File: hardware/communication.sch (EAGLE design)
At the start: 44 parts, among them J1 MICRO_USB_B_HIROSE_ZX62-B-5PA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, SW1 TVAF06-A020B-R, U2 NJM12888F, X1 FA-238

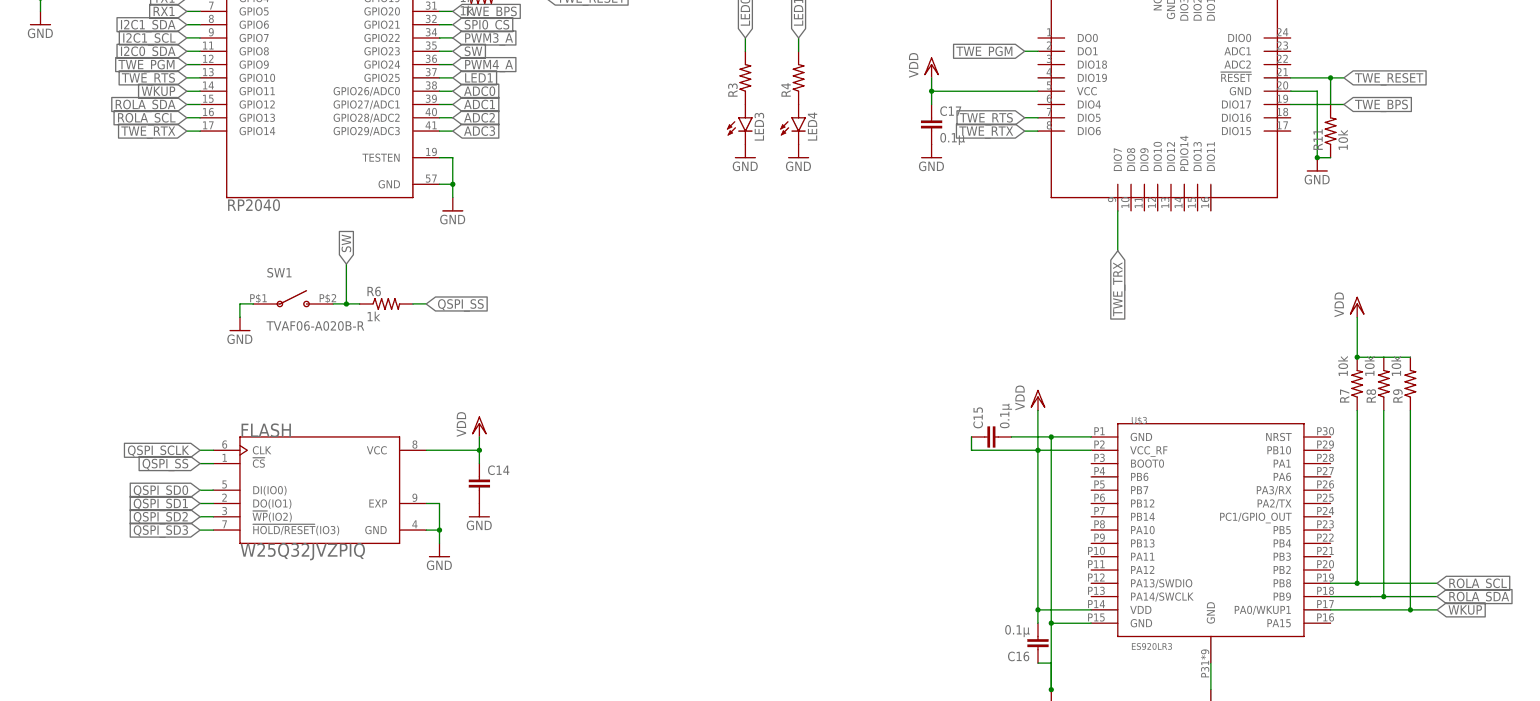
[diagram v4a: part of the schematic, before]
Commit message: 変更点: communication_LoRaをUART接続に変換 gnss_GPSのRTX接続およびRESETの追加
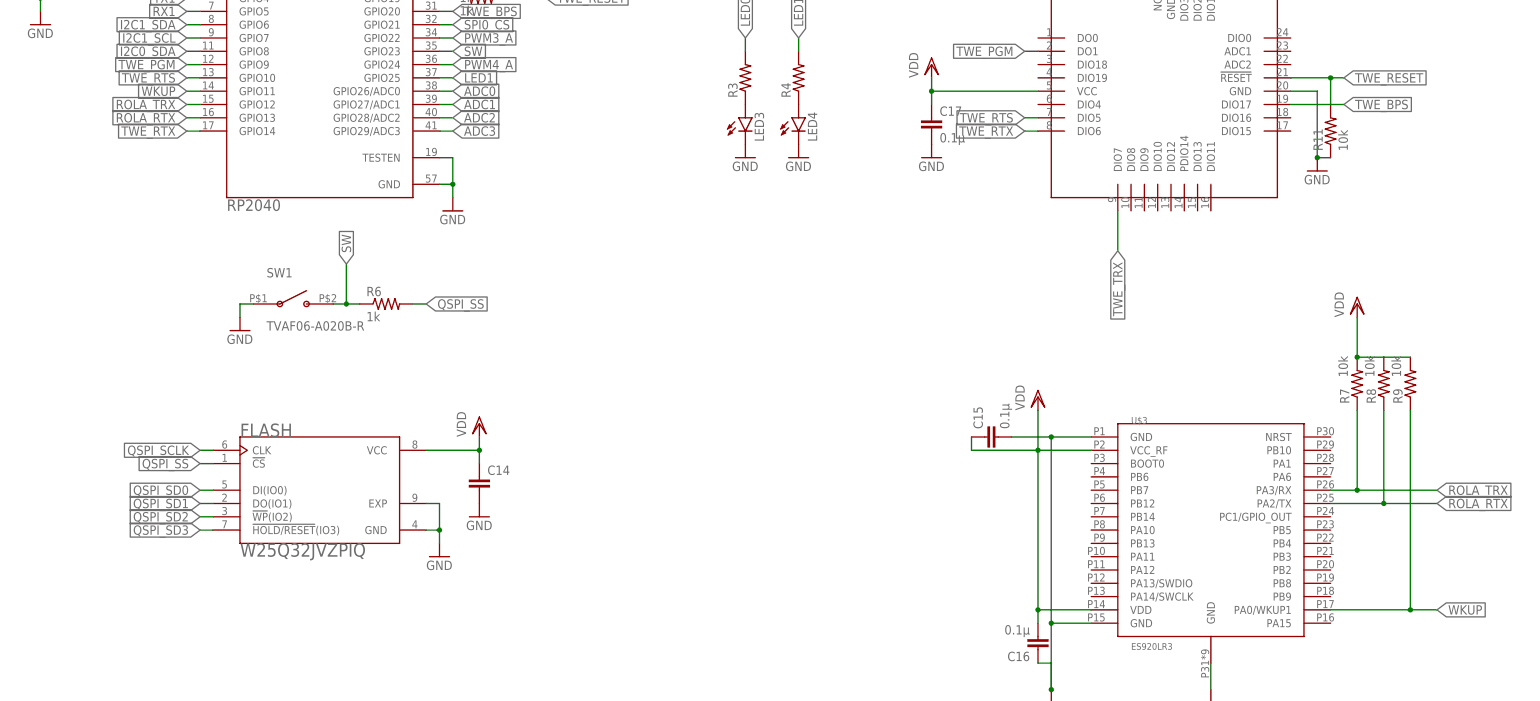
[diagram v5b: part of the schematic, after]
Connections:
- removed net ROLA_SCL: R7.1, RP1.GPIO13, U$3.PB8
- removed net ROLA_SDA: R8.1, RP1.GPIO12, U$3.PB9
- new net ROLA_RTX: R8.1, RP1.GPIO13, U$3.PA2/TX
- new net ROLA_TRX: R7.1, RP1.GPIO12, U$3.PA3/RX
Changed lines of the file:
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@@
-</segment>
-</net>
-<net name="ROLA_SCL" class="0">
-<segment>
-<pinref part="R7" gate="G$1" pin="1"/>
-<pinref part="U$3" gate="G$1" pin="PB8"/>
-<wire x1="248.92" y1="-25.4" x2="254" y2="-25.4" width="0.1524" layer="91"/>
-<label x="269.24" y="-25.4" size="1.778" layer="95" xref="yes"/>
-<wire x1="254" y1="-25.4" x2="269.24" y2="-25.4" width="0.1524" layer="91"/>
-<wire x1="254" y1="7.62" x2="254" y2="-25.4" width="0.1524" layer="91"/>
-<junction x="254" y="-25.4"/>
-</segment>
-<segment>
-<pinref part="RP1" gate="G$1" pin="GPIO13"/>
-<wire x1="33.02" y1="63.5" x2="30.48" y2="63.5" width="0.1524" layer="91"/>
-<label x="30.48" y="63.5" size="1.778" layer="95" rot="R180" xref="yes"/>
-</segment>
-</net>
-<net name="ROLA_SDA" class="0">
-<segment>
-<pinref part="R8" gate="G$1" pin="1"/>
-<pinref part="U$3" gate="G$1" pin="PB9"/>
-<wire x1="248.92" y1="-27.94" x2="256.54" y2="-27.94" width="0.1524" layer="91"/>
-<label x="269.24" y="-27.94" size="1.778" layer="95" xref="yes"/>
-<wire x1="259.08" y1="-27.94" x2="269.24" y2="-27.94" width="0.1524" layer="91"/>
-<wire x1="259.08" y1="7.62" x2="259.08" y2="-27.94" width="0.1524" layer="91"/>
-<wire x1="259.08" y1="-27.94" x2="256.54" y2="-27.94" width="0.1524" layer="91"/>
-<junction x="259.08" y="-27.94"/>
-</segment>
-<segment>
-<pinref part="RP1" gate="G$1" pin="GPIO12"/>
-<wire x1="33.02" y1="66.04" x2="30.48" y2="66.04" width="0.1524" layer="91"/>
-<label x="30.48" y="66.04" size="1.778" layer="95" rot="R180" xref="yes"/>
 </segment>
 </net>
@@
 </segment>
 </net>
+<net name="ROLA_TRX" class="0">
+<segment>
+<pinref part="U$3" gate="G$1" pin="PA3/RX"/>
+<wire x1="248.92" y1="-7.62" x2="254" y2="-7.62" width="0.1524" layer="91"/>
+<pinref part="R7" gate="G$1" pin="1"/>
+<wire x1="254" y1="-7.62" x2="269.24" y2="-7.62" width="0.1524" layer="91"/>
+<wire x1="254" y1="7.62" x2="254" y2="-7.62" width="0.1524" layer="91"/>
+<junction x="254" y="-7.62"/>
+<label x="269.24" y="-7.62" size="1.778" layer="95" xref="yes"/>
+</segment>
+<segment>
+<pinref part="RP1" gate="G$1" pin="GPIO12"/>
+<wire x1="33.02" y1="66.04" x2="30.48" y2="66.04" width="0.1524" layer="91"/>
+<label x="30.48" y="66.04" size="1.778" layer="95" rot="R180" xref="yes"/>
+</segment>
+</net>
+<net name="ROLA_RTX" class="0">
+<segment>
+<pinref part="U$3" gate="G$1" pin="PA2/TX"/>
+<wire x1="248.92" y1="-10.16" x2="259.08" y2="-10.16" width="0.1524" layer="91"/>
+<pinref part="R8" gate="G$1" pin="1"/>
+<wire x1="259.08" y1="-10.16" x2="269.24" y2="-10.16" width="0.1524" layer="91"/>
+<wire x1="259.08" y1="7.62" x2="259.08" y2="-10.16" width="0.1524" layer="91"/>
+<junction x="259.08" y="-10.16"/>
+<label x="269.24" y="-10.16" size="1.778" layer="95" xref="yes"/>
+</segment>
+<segment>
+<pinref part="RP1" gate="G$1" pin="GPIO13"/>
+<wire x1="33.02" y1="63.5" x2="30.48" y2="63.5" width="0.1524" layer="91"/>
+<label x="30.48" y="63.5" size="1.778" layer="95" rot="R180" xref="yes"/>
+</segment>
+</net>

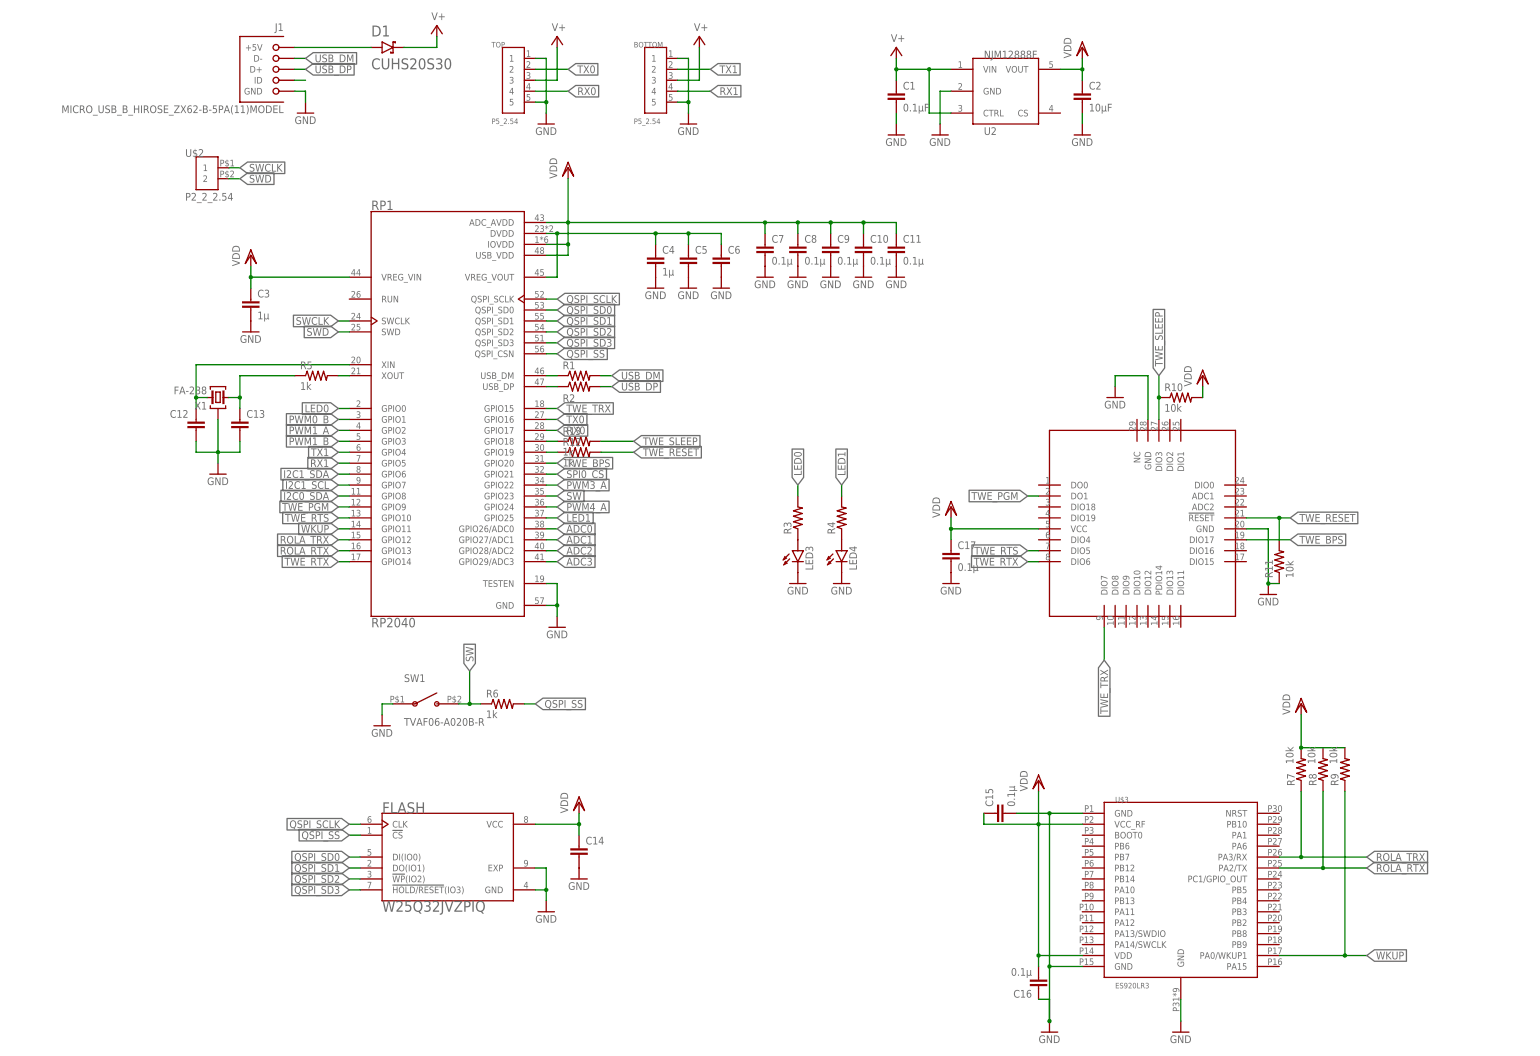
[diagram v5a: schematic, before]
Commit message: べたGND前です。esp32のschはノータッチなのでここに上がってないです。よろしくお願いします。
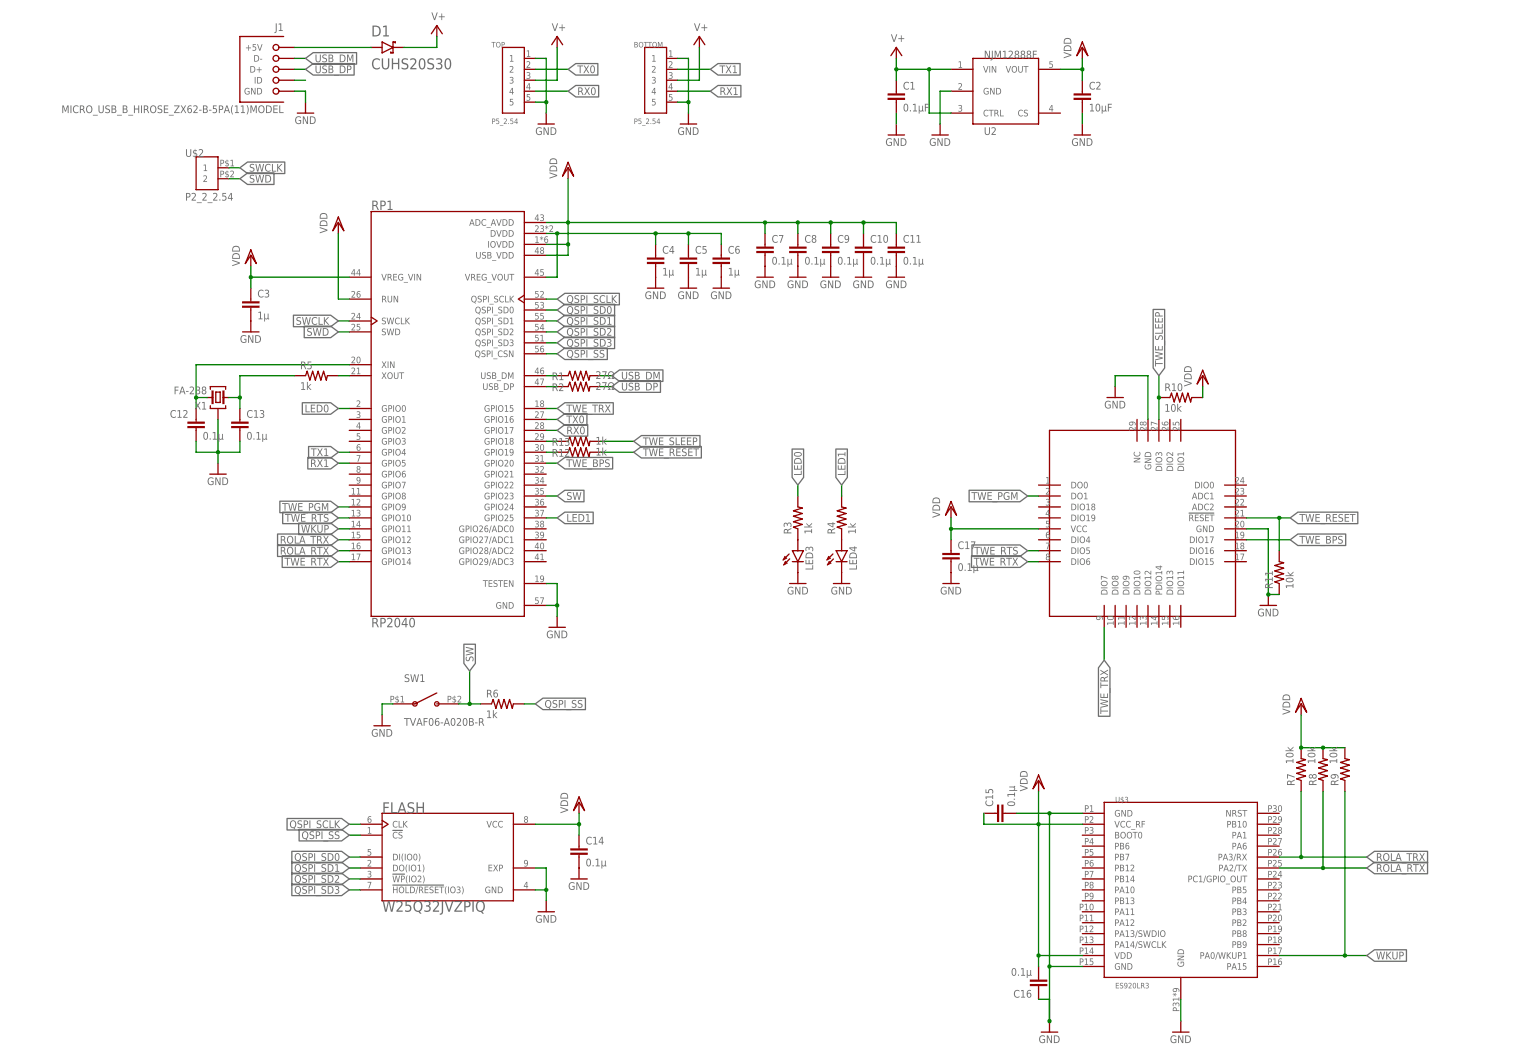
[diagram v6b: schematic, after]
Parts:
- C12, C13, C14: value (none) -> 0.1μ
- C5, C6: value (none) -> 1μ
- R1, R2: value (none) -> 27Ω
- R3, R4: value (none) -> 1k
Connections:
- removed net ADC0: RP1.GPIO26/ADC0
- removed net ADC1: RP1.GPIO27/ADC1
- removed net ADC2: RP1.GPIO28/ADC2
- removed net ADC3: RP1.GPIO29/ADC3
- removed net I2C0_SDA: RP1.GPIO8
- removed net I2C1_SCL: RP1.GPIO7
- removed net I2C1_SDA: RP1.GPIO6
- removed net PWM0_B: RP1.GPIO1
- removed net PWM1_A: RP1.GPIO2
- removed net PWM1_B: RP1.GPIO3
- removed net PWM3_A: RP1.GPIO22
- removed net PWM4_A: RP1.GPIO24
- removed net SPI0_CS: RP1.GPIO21
- net VDD: now also RP1.RUN
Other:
- moved on the sheet: R11

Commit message: LoRa ResetとTWELITE TX&RXの引き出しピンを追加
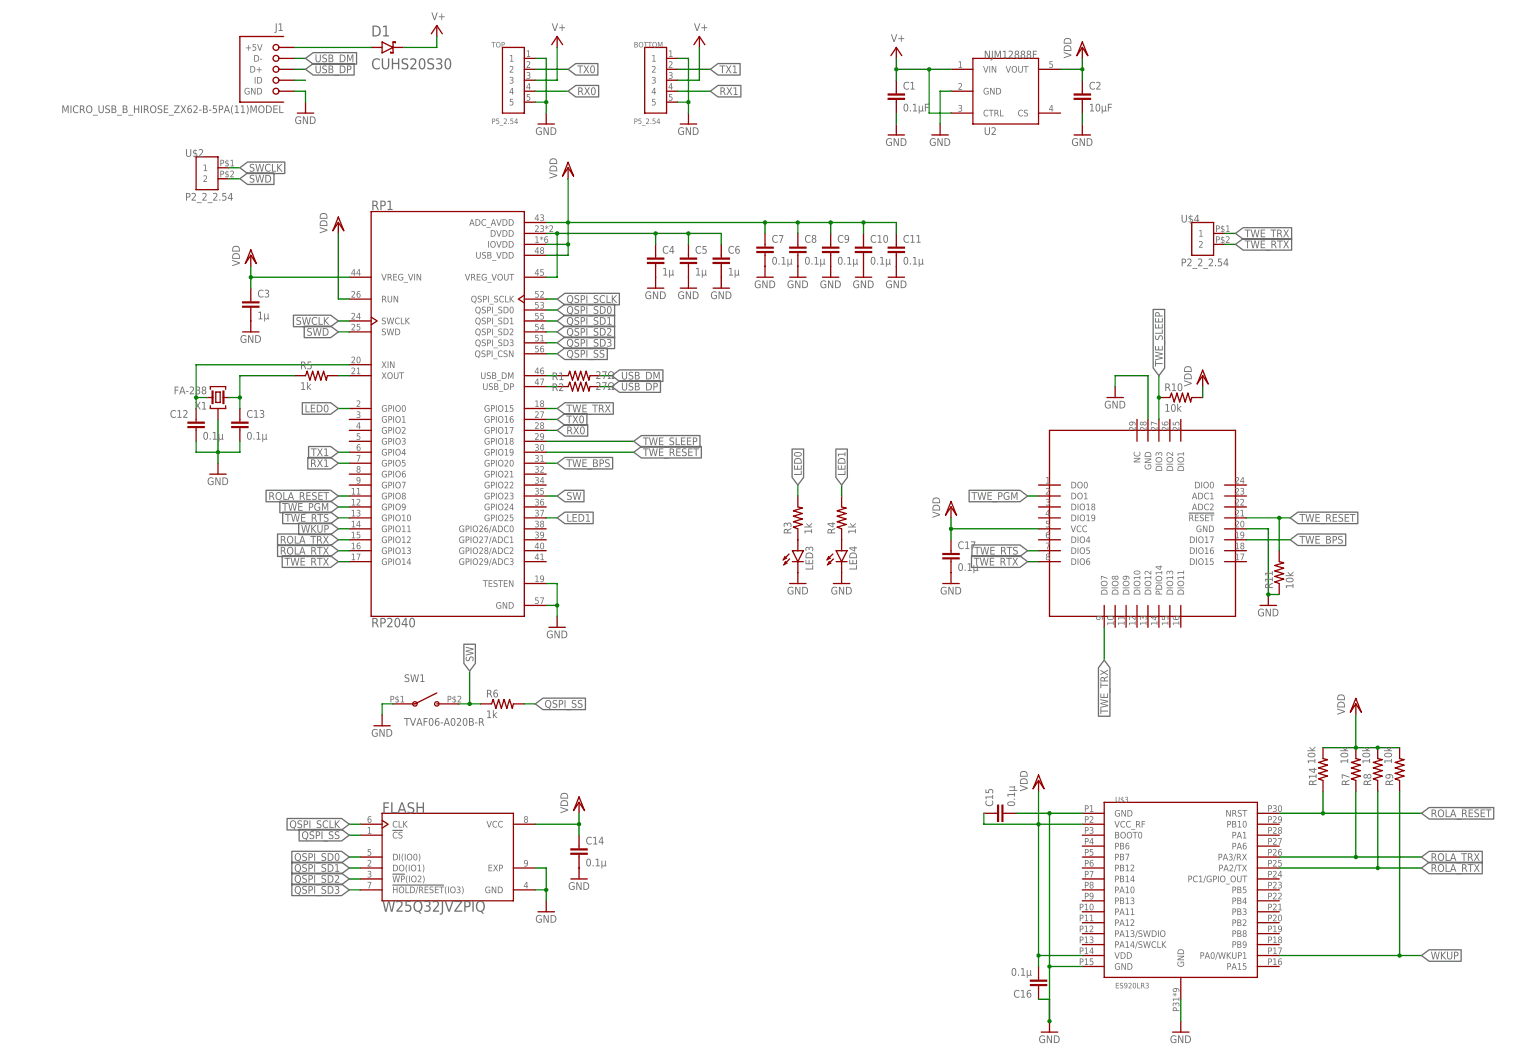
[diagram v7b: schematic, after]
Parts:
- removed R12, R13: 1k, rcl:R-US_R0402
- added R14: 10k, rcl:R-US_R0402
- added U$4: P2_2_2.54, pins:P2_2_2.54
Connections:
- new net ROLA_!RESET!: R14.1, RP1.GPIO8, U$3.NRST
- net TWE_RESET: no longer R12.1, R12.2
- net TWE_RTX: now also U$4.2
- net TWE_SLEEP: no longer R13.1, R13.2
- net TWE_TRX: now also U$4.1
- net VDD: now also R14.2
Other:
- moved on the sheet: R7, R8, R9

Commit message: シルクを調整
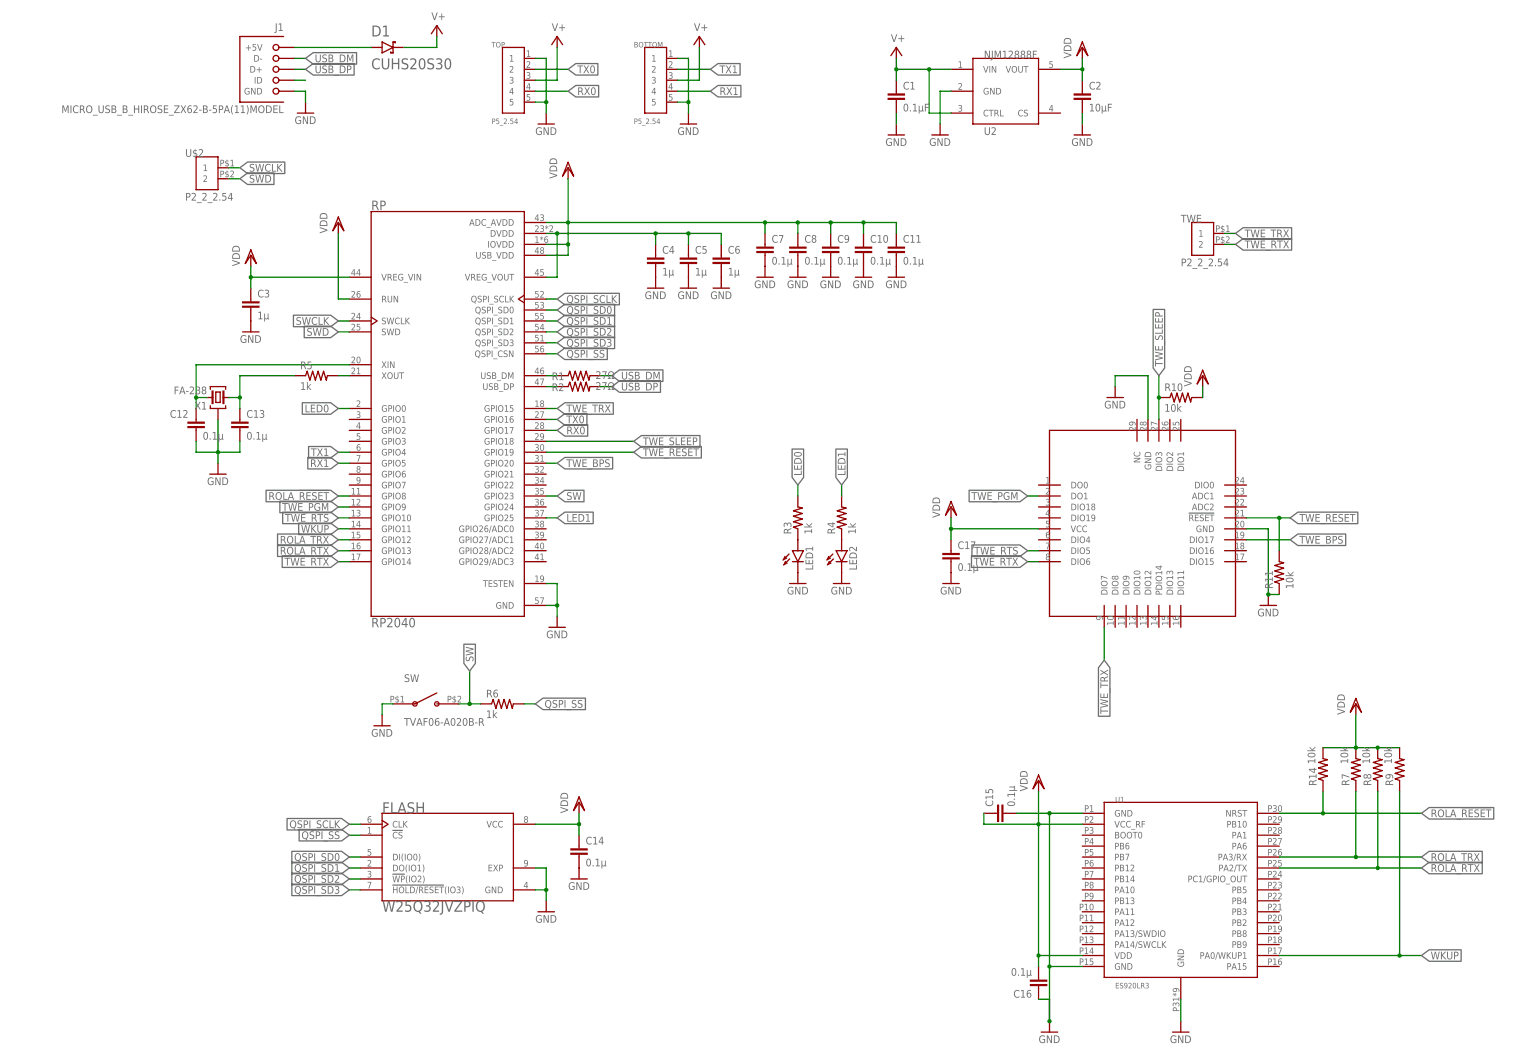
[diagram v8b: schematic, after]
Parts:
- renumbered LED3 to LED1, LED4 to LED2, RP1 to RP, SW1 to SW, U$3 to U1, U$4 to TWE
